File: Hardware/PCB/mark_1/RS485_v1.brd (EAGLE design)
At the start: 22.9 x 15.2 mm, 5 parts

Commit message: 
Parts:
- renumbered U$1 to IC1
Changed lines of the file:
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@@
 </autorouter>
 <elements>
-<element name="U$1" library="mark_1" package="SO08" value="MAX485" x="14.605" y="7.62" rot="MR270"/>
+<element name="IC1" library="mark_1" package="SO08" value="MAX485" x="14.605" y="7.62" rot="MR270"/>
 <element name="R1" library="mark_1" package="R0805" value="" x="8.255" y="7.62" rot="MR90"/>
 <element name="X1" library="mark_1" package="W237-103" value="" x="5.715" y="7.62" rot="R270"/>
@@
 <signals>
 <signal name="+5V">
-<contactref element="U$1" pad="8"/>
+<contactref element="IC1" pad="8"/>
 <contactref element="C1" pad="1"/>
 <contactref element="JP1" pad="1"/>
@@
 </signal>
 <signal name="GND">
-<contactref element="U$1" pad="5"/>
+<contactref element="IC1" pad="5"/>
 <contactref element="X1" pad="3"/>
 <contactref element="C1" pad="2"/>
@@
 </signal>
 <signal name="TXD">
-<contactref element="U$1" pad="1"/>
+<contactref element="IC1" pad="1"/>
 <contactref element="JP1" pad="2"/>
 <wire x1="17.2212" y1="9.525" x2="18.415" y2="9.525" width="0.4064" layer="16"/>
@@
 </signal>
 <signal name="RXD">
-<contactref element="U$1" pad="4"/>
+<contactref element="IC1" pad="4"/>
 <contactref element="JP1" pad="4"/>
 <wire x1="17.2212" y1="5.715" x2="18.415" y2="5.715" width="0.4064" layer="16"/>
@@
 </signal>
 <signal name="EN">
-<contactref element="U$1" pad="3"/>
-<contactref element="U$1" pad="2"/>
+<contactref element="IC1" pad="3"/>
+<contactref element="IC1" pad="2"/>
 <contactref element="JP1" pad="3"/>
 <wire x1="17.2212" y1="8.255" x2="17.2212" y2="8.1788" width="0.4064" layer="16"/>
@@
 </signal>
 <signal name="N$1">
-<contactref element="U$1" pad="7"/>
+<contactref element="IC1" pad="7"/>
 <contactref element="R1" pad="2"/>
 <contactref element="X1" pad="1"/>
@@
 </signal>
 <signal name="N$2">
-<contactref element="U$1" pad="6"/>
+<contactref element="IC1" pad="6"/>
 <contactref element="R1" pad="1"/>
 <contactref element="X1" pad="2"/>

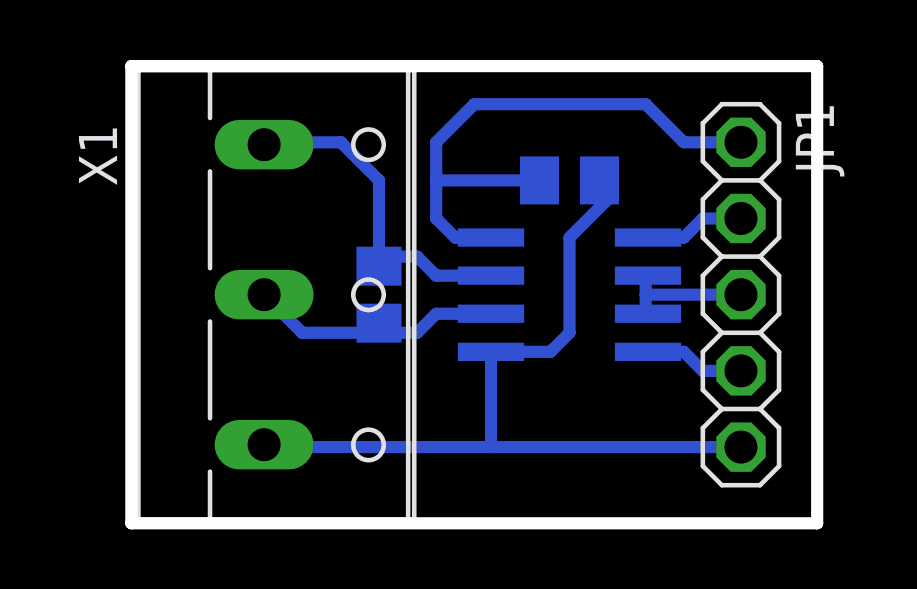
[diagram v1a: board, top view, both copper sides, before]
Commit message: 
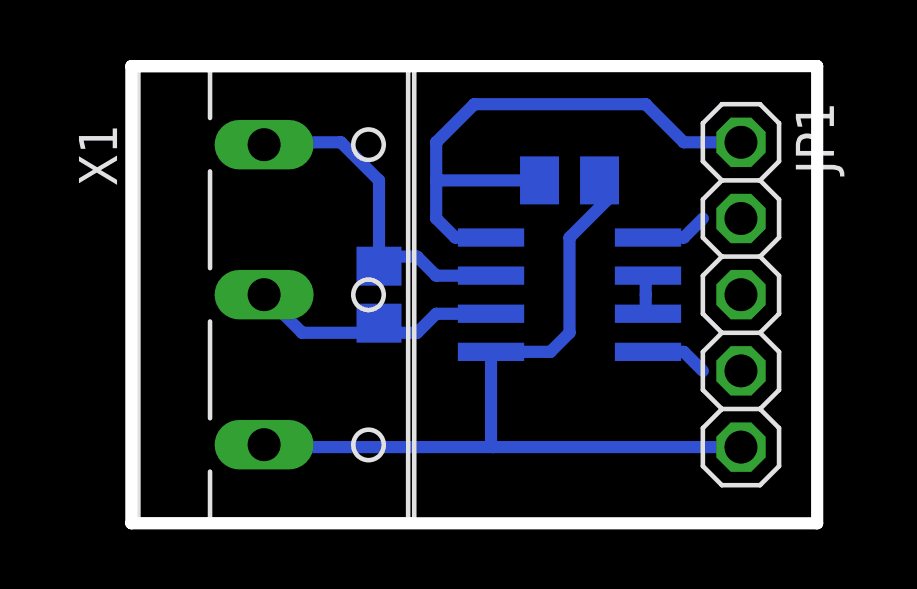
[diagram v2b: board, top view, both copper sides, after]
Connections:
- net N$1 renamed B
- net N$2 renamed A
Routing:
- net EN: track 4.58 -> 1.41 mm
- net TXD: track 3.36 -> 2.09 mm
- net RXD: track 3.36 -> 2.09 mm
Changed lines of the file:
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@@
 <signal name="TXD">
 <contactref element="IC1" pad="1"/>
-<contactref element="JP1" pad="2"/>
 <wire x1="17.2212" y1="9.525" x2="18.415" y2="9.525" width="0.4064" layer="16"/>
 <wire x1="18.415" y1="9.525" x2="19.05" y2="10.16" width="0.4064" layer="16"/>
-<wire x1="19.05" y1="10.16" x2="20.32" y2="10.16" width="0.4064" layer="16"/>
+<contactref element="JP1" pad="2"/>
+<wire x1="19.05" y1="10.16" x2="20.32" y2="10.16" width="0" layer="19" extent="16-16"/>
 </signal>
 <signal name="RXD">
 <contactref element="IC1" pad="4"/>
-<contactref element="JP1" pad="4"/>
 <wire x1="17.2212" y1="5.715" x2="18.415" y2="5.715" width="0.4064" layer="16"/>
 <wire x1="18.415" y1="5.715" x2="19.05" y2="5.08" width="0.4064" layer="16"/>
-<wire x1="19.05" y1="5.08" x2="20.32" y2="5.08" width="0.4064" layer="16"/>
+<contactref element="JP1" pad="4"/>
+<wire x1="19.05" y1="5.08" x2="20.32" y2="5.08" width="0" layer="19" extent="16-16"/>
 </signal>
 <signal name="EN">
 <contactref element="IC1" pad="3"/>
 <contactref element="IC1" pad="2"/>
-<contactref element="JP1" pad="3"/>
 <wire x1="17.2212" y1="8.255" x2="17.2212" y2="8.1788" width="0.4064" layer="16"/>
-<wire x1="17.145" y1="7.62" x2="20.32" y2="7.62" width="0.4064" layer="16"/>
 <wire x1="17.145" y1="7.62" x2="17.145" y2="8.1788" width="0.4064" layer="16"/>
 <wire x1="17.145" y1="8.1788" x2="17.2212" y2="8.255" width="0.4064" layer="16"/>
 <wire x1="17.145" y1="7.62" x2="17.145" y2="7.0612" width="0.4064" layer="16"/>
 <wire x1="17.145" y1="7.0612" x2="17.2212" y2="6.985" width="0.4064" layer="16"/>
+<contactref element="JP1" pad="3"/>
+<wire x1="17.2212" y1="8.1788" x2="20.32" y2="7.62" width="0" layer="19" extent="16-16"/>
 </signal>
-<signal name="N$1">
+<signal name="B">
 <contactref element="IC1" pad="7"/>
 <contactref element="R1" pad="2"/>
@@
 <wire x1="4.505" y1="12.7" x2="4.425" y2="12.62" width="0.4064" layer="16"/>
 </signal>
-<signal name="N$2">
+<signal name="A">
 <contactref element="IC1" pad="6"/>
 <contactref element="R1" pad="1"/>
